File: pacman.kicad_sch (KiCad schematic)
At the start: 135 parts, among them J1 RESET, J2 BOOT, SW1 MX_LED, SW10 MX_LED, SW11 MX_LED, SW12 MX_LED, SW13 MX_LED, SW14 MX_LED, SW15 MX_LED, SW16 MX_LED, SW17 MX_LED, SW18 MX_LED, SW19 MX_LED, SW2 MX_LED, SW20 MX_LED, SW21 MX_LED, SW22 MX_LED, SW23 MX_LED, SW24 MX_LED, SW25 MX_LED, SW26 MX_LED, SW27 MX_LED, SW28 MX_LED, SW29 MX_LED, SW3 MX_LED, SW30 MX_LED, SW31 MX_LED, SW32 MX_LED, SW33 MX_LED, SW34 MX_LED, SW35 MX_LED, SW36 MX_LED, SW37 MX_LED, SW38 MX_LED, SW39 MX_LED, SW4 MX_LED, SW40 MX_LED, SW41 MX_LED, SW42_2 MX_LED, SW44 MX_LED, SW45 MX_LED, SW46 MX_LED, SW47 MX_LED, SW48 MX_LED, SW5 MX_LED, SW6 MX_LED, SW7 MX_LED, SW8 MX_LED, SW9 MX_LED, U1 NCP1117-3.3_SOT223, U2 RP2040, U3 W25Q128JVS, Y1 12MHz

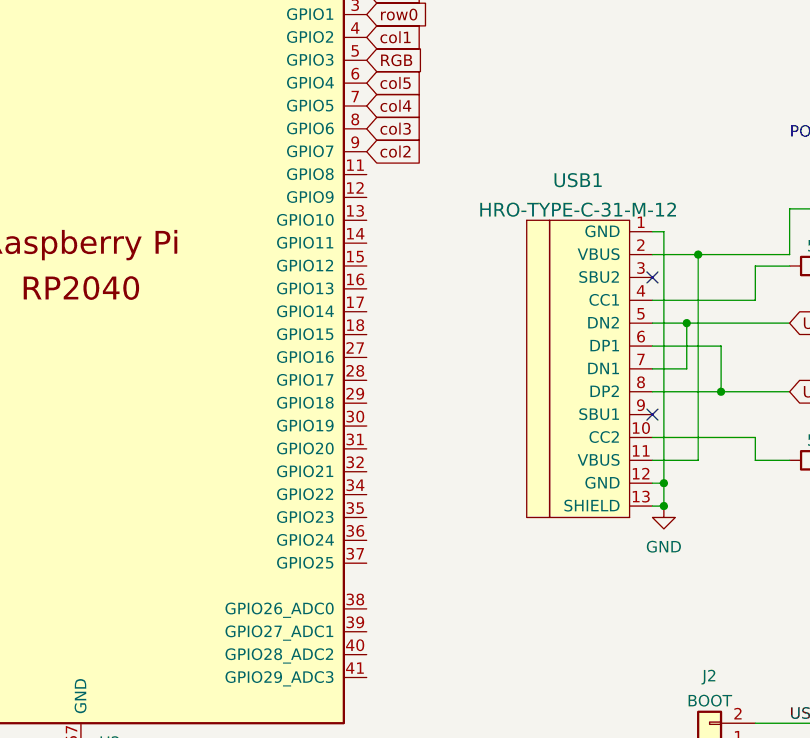
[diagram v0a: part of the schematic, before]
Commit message: Fix unconnected rows
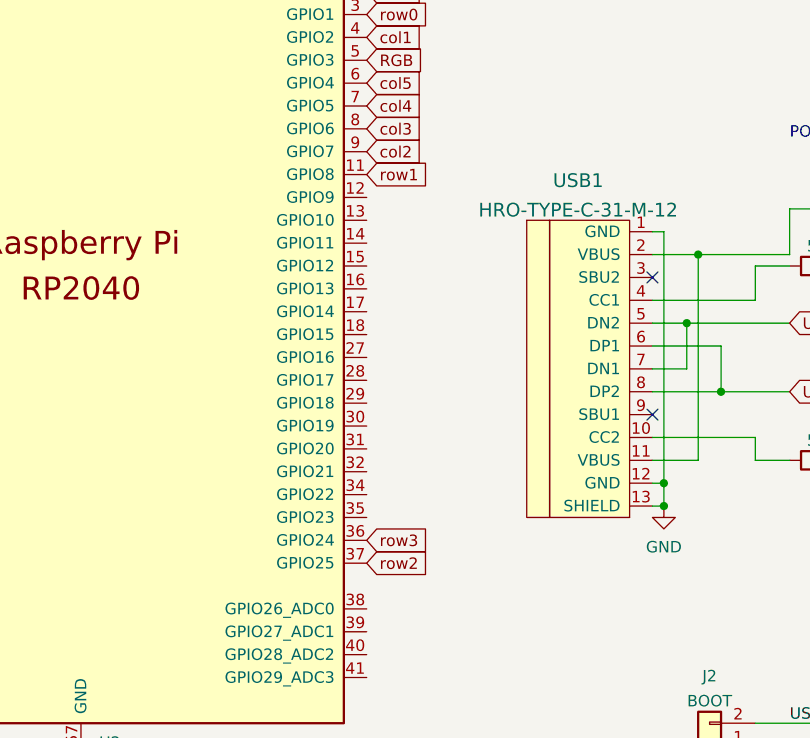
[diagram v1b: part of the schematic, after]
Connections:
- net row1: now also U2.11 (GPIO8)
- net row2: now also U2.37 (GPIO25)
- net row3: now also U2.36 (GPIO24)
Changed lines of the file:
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@@
+    )
+  )
+  (global_label "row2" (shape input) (at 100.33 138.43 0) (fields_autoplaced)
+    (effects (font (size 1.27 1.27)) (justify left))
+    (property "Intersheet References" "${INTERSHEET_REFS}" (id 0) (at 107.2183 138.5094 0)
+      (effects (font (size 1.27 1.27)) (justify left) hide)
     )
   )
@@
     (effects (font (size 1.27 1.27)) (justify left))
     (property "Intersheet References" "${INTERSHEET_REFS}" (id 0) (at 107.2183 77.3906 0)
+      (effects (font (size 1.27 1.27)) (justify left) hide)
+    )
+  )
+  (global_label "row3" (shape input) (at 100.33 135.89 0) (fields_autoplaced)
+    (effects (font (size 1.27 1.27)) (justify left))
+    (property "Intersheet References" "${INTERSHEET_REFS}" (id 0) (at 107.2183 135.9694 0)
       (effects (font (size 1.27 1.27)) (justify left) hide)
     )
@@
       (effects (font (size 1.27 1.27)) (justify left) hide)
     )
+  )
+  (global_label "row1" (shape input) (at 100.33 95.25 0) (fields_autoplaced)
+    (effects (font (size 1.27 1.27)) (justify left))
+    (property "Intersheet References" "${INTERSHEET_REFS}" (id 0) (at 107.2183 95.3294 0)
+      (effects (font (size 1.27 1.27)) (justify left) hide)
+    )

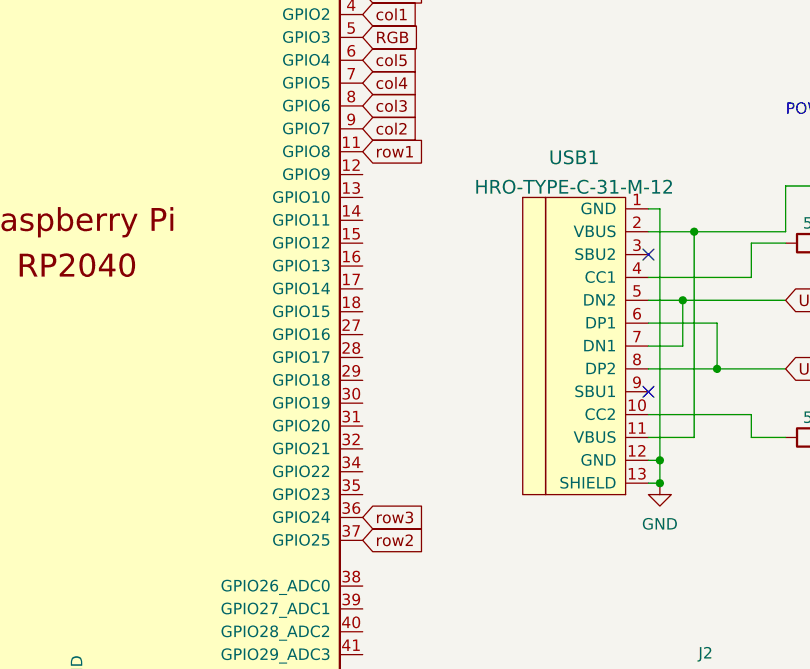
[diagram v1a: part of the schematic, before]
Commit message: Fix unconnected Column
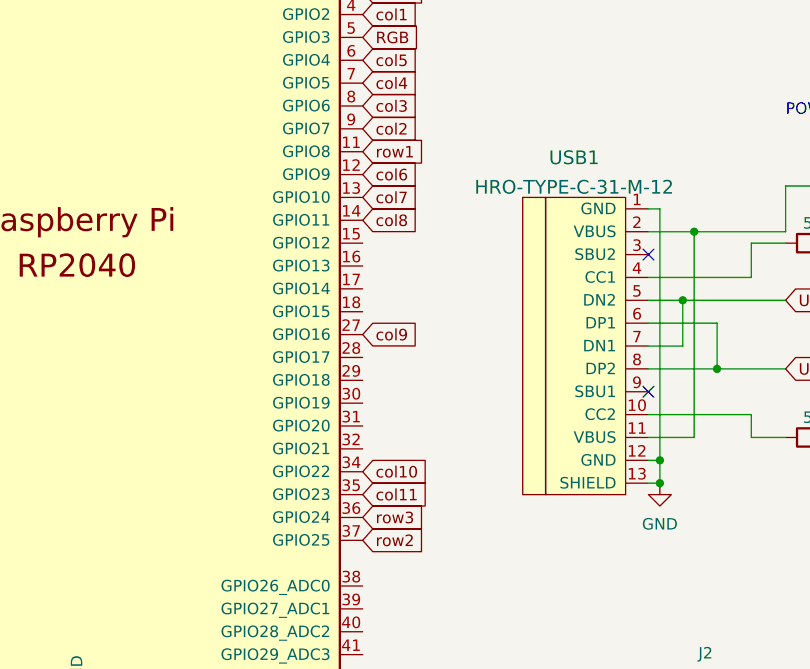
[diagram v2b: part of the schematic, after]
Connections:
- net col10: now also U2.34 (GPIO22)
- net col11: now also U2.35 (GPIO23)
- net col6: now also U2.12 (GPIO9)
- net col7: now also U2.13 (GPIO10)
- net col8: now also U2.14 (GPIO11)
- net col9: now also U2.27 (GPIO16)
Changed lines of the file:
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@@
+    )
+  )
+  (global_label "col7" (shape input) (at 100.33 100.33 0) (fields_autoplaced)
+    (effects (font (size 1.27 1.27)) (justify left))
+    (property "Intersheet References" "${INTERSHEET_REFS}" (id 0) (at 106.8555 100.2506 0)
+      (effects (font (size 1.27 1.27)) (justify left) hide)
     )
   )
@@
     )
   )
+  (global_label "col8" (shape input) (at 100.33 102.87 0) (fields_autoplaced)
+    (effects (font (size 1.27 1.27)) (justify left))
+    (property "Intersheet References" "${INTERSHEET_REFS}" (id 0) (at 106.8555 102.7906 0)
+      (effects (font (size 1.27 1.27)) (justify left) hide)
+    )
+  )
   (global_label "col6" (shape input) (at 419.1 25.4 90) (fields_autoplaced)
     (effects (font (size 1.27 1.27)) (justify left))
@@
     )
   )
+  (global_label "col11" (shape input) (at 100.33 133.35 0) (fields_autoplaced)
+    (effects (font (size 1.27 1.27)) (justify left))
+    (property "Intersheet References" "${INTERSHEET_REFS}" (id 0) (at 108.065 133.2706 0)
+      (effects (font (size 1.27 1.27)) (justify left) hide)
+    )
+  )
   (global_label "col1" (shape input) (at 100.33 80.01 0) (fields_autoplaced)
     (effects (font (size 1.27 1.27)) (justify left))
@@
     )
   )
+  (global_label "col9" (shape input) (at 100.33 115.57 0) (fields_autoplaced)
+    (effects (font (size 1.27 1.27)) (justify left))
+    (property "Intersheet References" "${INTERSHEET_REFS}" (id 0) (at 106.8555 115.4906 0)
+      (effects (font (size 1.27 1.27)) (justify left) hide)
+    )
+  )
   (global_label "col9" (shape input) (at 495.3 25.4 90) (fields_autoplaced)
     (effects (font (size 1.27 1.27)) (justify left))
@@
     )
   )
+  (global_label "col6" (shape input) (at 100.33 97.79 0) (fields_autoplaced)
+    (effects (font (size 1.27 1.27)) (justify left))
+    (property "Intersheet References" "${INTERSHEET_REFS}" (id 0) (at 106.8555 97.7106 0)
+      (effects (font (size 1.27 1.27)) (justify left) hide)
+    )
+  )
   (global_label "col2" (shape input) (at 317.5 25.4 90) (fields_autoplaced)
     (effects (font (size 1.27 1.27)) (justify left))
@@
       (effects (font (size 1.27 1.27)) (justify left) hide)
     )
+  )
+  (global_label "col10" (shape input) (at 100.33 130.81 0) (fields_autoplaced)
+    (effects (font (size 1.27 1.27)) (justify left))
+    (property "Intersheet References" "${INTERSHEET_REFS}" (id 0) (at 108.065 130.7306 0)
+      (effects (font (size 1.27 1.27)) (justify left) hide)
+    )

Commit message: Add Encoder
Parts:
- added SW42, SW43: RotaryEncoder_Switch, Keebio-Parts:RotaryEncoder_EC11, symbol Device:RotaryEncoder_Switch
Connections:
- net GND: now also SW42.C, SW43.C
- net col0: now also SW42.S2
- net col11: now also SW43.S2
- net at D1.2 (A), SW1.2: now also SW42.S1
- net ENC_1_A: now reaches U2.17 (GPIO14)
- net ENC_1_A: now also SW43.A
- net ENC_1_B: now reaches U2.18 (GPIO15)
- net ENC_1_B: now also SW43.B
- net ENC_0_B: now reaches U2.31 (GPIO20)
- net ENC_0_B: now also SW42.B
- net ENC_0_A: now reaches U2.32 (GPIO21)
- net ENC_0_A: now also SW42.A
- net at D12.2 (A), SW12.2: now also SW43.S1
